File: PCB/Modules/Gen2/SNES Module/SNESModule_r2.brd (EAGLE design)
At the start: 35.1 x 66.1 mm, 25 parts, among them IC1 SN65HVD31DR, IC2 PCA9517, IC3 LM3480-5.0

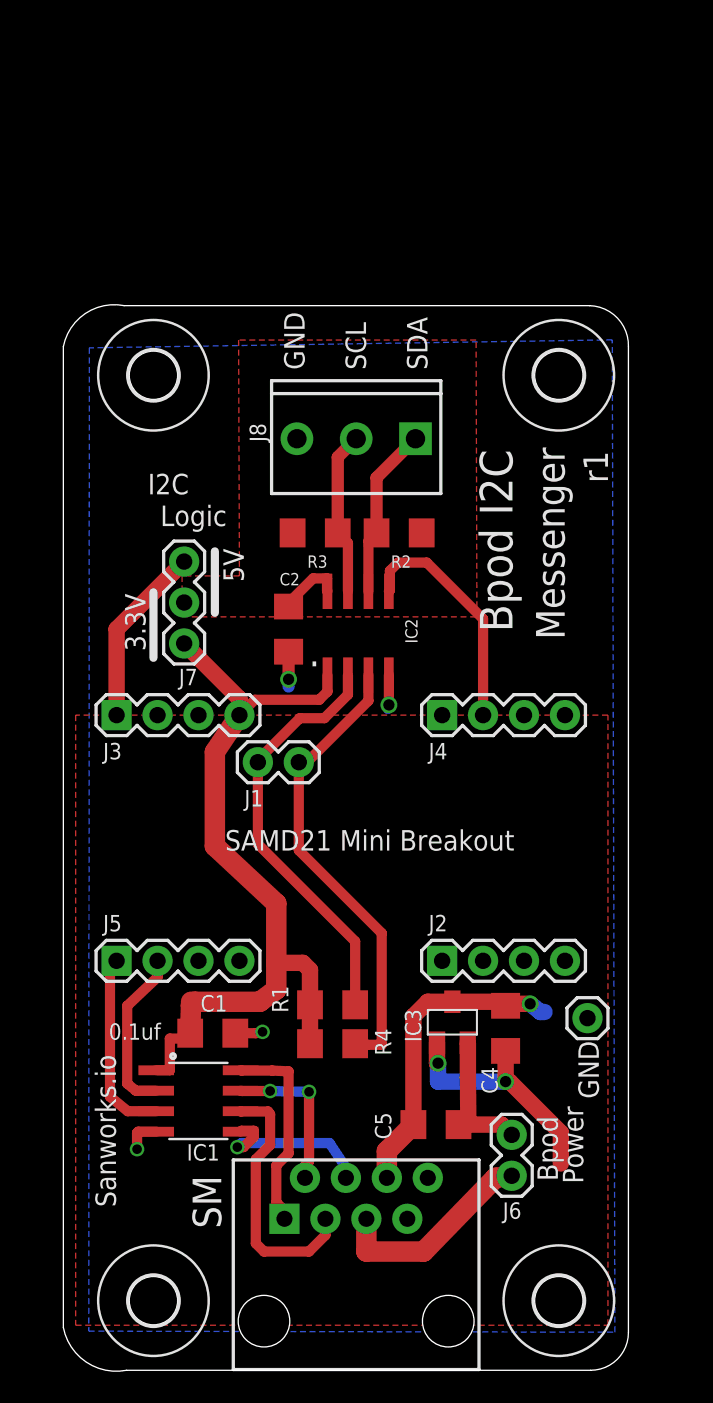
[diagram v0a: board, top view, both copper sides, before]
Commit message: -Critical Update for modules with optional RJ45 power (ValveDriver, I2C, SNES and DDS); new PCB designs add a diode to prevent USB power from entering output pin of 5V regulator, when RJ45 (state machine) power is not connected. This update greatly reduces unnecessary power consumption and heat dissipation. If you built a board using the previous designs, please Email a photo of your board to Sanworks support for a free upgrade. -Updated component names on some boards and on web BOMs to avoid skipping parts -Renamed Gen2 module PCB folder from '0.7' to 'Gen2' -Retired pocket state machine (to be replaced with Bpod State Machine r1)
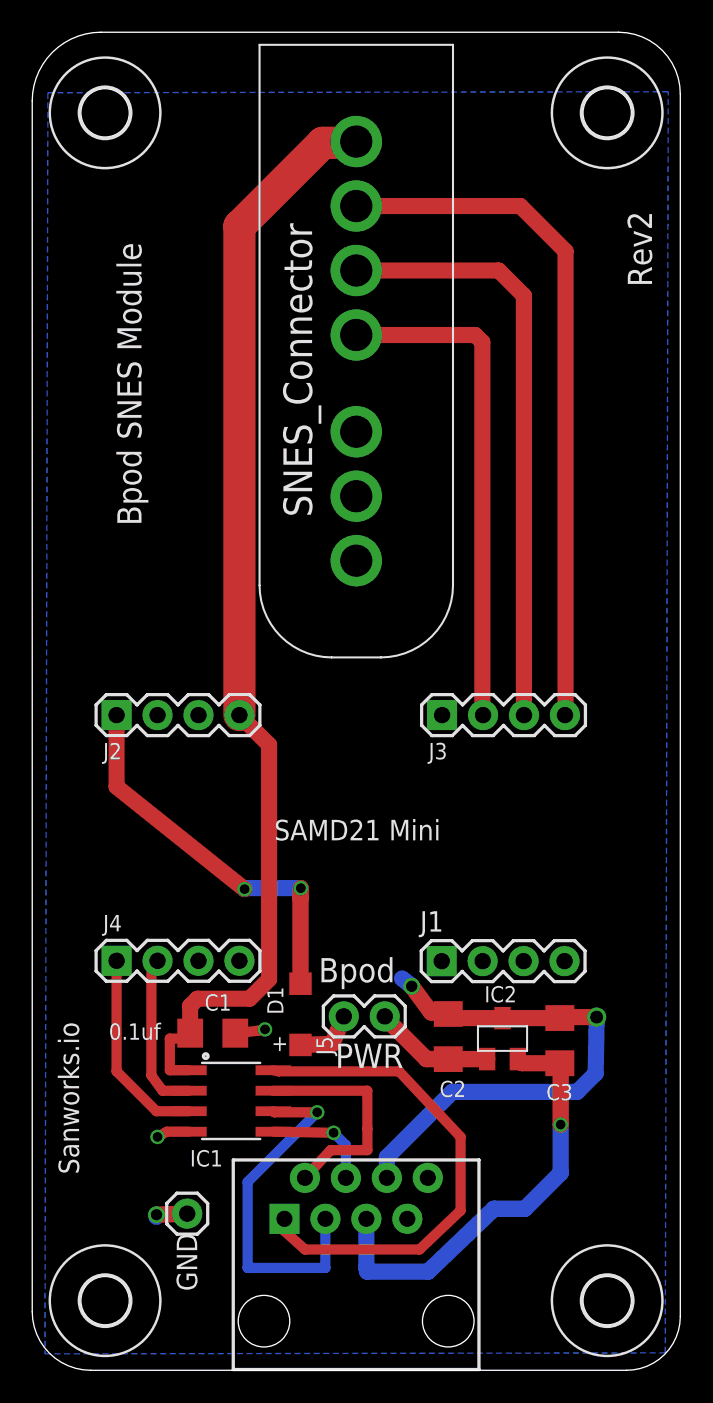
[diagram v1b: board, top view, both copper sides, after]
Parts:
- removed C4, C5: 0.1uf, SparkFun-Capacitors:1206
- removed IC3: LM3480-5.0, regulators:SOT-23-3
- removed J6: (no value), SparkFun-Connectors:1X02
- removed J8: (no value), SparkFun-Connectors:SCREWTERMINAL-3.5MM-3_LOCK.007S
- removed JG: (no value), SparkFun-Connectors:1X01
- removed R1, R2, R3, R4: 10k, SparkFun-Resistors:1206
- added C3: 0.1uf, SparkFun-Capacitors:1206
- added D1: MBR0520LT, diode:SOD123
- added U$2: SNES_CONNECTOR, JoshParts10:SNES_CONNECTOR
- IC2: value PCA9517 -> LM3480-5.0; device PCA9517:SO-08 -> regulators:SOT-23-3
- J1: device SparkFun-Connectors:1X02@1 -> SparkFun-Connectors:1X04
- J5: device SparkFun-Connectors:1X04 -> SparkFun-Connectors:1X02
- J7: device SparkFun-Connectors:1X03 -> SparkFun-Connectors:1X01
- moved J7 35.4 mm to (6.41, 9.72), turned to 0 degrees
- moved C2 27.1 mm to (22.6, 20.7)
- moved IC2 26.7 mm to (26.0, 20.6)
- moved J2 25.3 mm to (2.03, 40.6)
- moved J4 25.3 mm to (2.03, 25.4)
- moved J3 20.2 mm to (22.2, 40.6)
- moved J5 17.0 mm to (18.7, 22.0), turned to 180 degrees
- moved J1 16.8 mm to (22.2, 25.4)
- moved H3 16.6 mm to (32.5, 78.0)
- moved H4 16.6 mm to (1.32, 78.0)
- moved H2 3.00 mm to (32.5, 4.32)
- moved H1 3.00 mm to (1.32, 4.32)
- moved IC1 2.03 mm to (9.14, 16.7)
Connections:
- removed net N$12: C2.1, IC2.8, J7.2, R2.2, R3.2
- removed net N$13: IC2.5, J4.2
- removed net N$14: IC2.6, J8.1, R2.1
- removed net N$15: IC2.7, J8.2, R3.1
- new net N$2: J3.3, U$2.LATCH
- new net N$3: J3.4, U$2.CLOCK
- net 5V: now also D1.C, J2.1; no longer C4.2, IC3.1, J3.1, J7.3
- net GND: now also C2.1, C3.1, IC2.3, J4.4, J7.1, U$2.GND; no longer C2.2, C4.1, C5.1, IC2.4, IC3.3, J5.4, J8.3, JG.1
- net N$1: now also J3.2, U$2.DATA; no longer J6.2, U$1.5
- net N$11: now also D1.A, J5.2; no longer IC2.3, J1.2, R4.1
- net N$26: now also C3.2, IC2.2, U$1.5; no longer C5.2, IC3.2, J6.1
- net N$4: now also J4.1; no longer J5.1
- net N$5: now also C2.2, IC2.1, J5.1; no longer IC2.2, J1.1, R1.1
- net N$6: now also J4.2; no longer J5.2
- net VCC: now also J2.4, U$2.V+; no longer IC2.1, J3.4, J7.1, R1.2, R4.2
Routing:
- net N$3: track 0.00 -> 42.9 mm
- net N$2: track 0.00 -> 37.1 mm
- net N$11: track 29.0 -> 3.83 mm
- net VCC: track 50.9 -> 70.1 mm
- net N$7: track 12.7 -> 31.0 mm
- net N$5: track 26.2 -> 7.78 mm
- net N$1: track 13.0 -> 31.2 mm
- net N$26: track 9.25 -> 27.3 mm, vias 0 -> 1
- net N$13: track 14.7 -> 0.00 mm
- net GND: track 27.8 -> 39.2 mm
- net N$14: track 10.7 -> 0.00 mm
- net N$15: track 10.2 -> 0.00 mm
- net N$9: track 16.3 -> 22.1 mm, vias 0 -> 1
- net N$12: track 4.51 -> 0.00 mm
- net N$8: track 9.69 -> 14.1 mm, vias 2 -> 0
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- removed copper zone on layer 1, net 5V
- removed copper zone on layer 1, net N$12
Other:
- board size 35.1 x 66.1 mm -> 40.2 x 83 mm
- board text added: "+"
- board text added: "Bpod SNES Module"
- board text added: "PWR"
- board text added: "Rev2"
- board text added: "SAMD21 Mini"
- board text added: "SNES_Connector"
- board text removed: "."
- board text removed: "3.3V"
- board text removed: "5V"
- board text removed: "Bpod I2C"
- board text removed: "I2C"
- board text removed: "Logic"
- board text removed: "Messenger"
- board text removed: "Power"
- board text removed: "SAMD21 Mini Breakout"
- board text removed: "SCL"
- board text removed: "SDA"
- board text removed: "SM"
- board text removed: "r1"
